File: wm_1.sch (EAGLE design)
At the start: 26 parts, among them IC2 DS1813-SMD, IC4 MEGA8-AI, T1 MMBT3904, T2 BT138-V, X1 MKDSN1,5/2-5,08, X2 MKDSN1,5/2-5,08

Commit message: wip
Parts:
- added R8, R9: 1k, rcl:R-EU_R1206
- added SJ1: (no value), MyLib:SOLDERJUMPERREFLOW
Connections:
- new net N$17: OK2.A, R8.1
- new net N$18: OK1.COL, R9.2, SJ1.1
- net +5V: now also R9.1
- net 485_R/W: now also R8.2; no longer OK2.A
- net GND: now also OK1.EMI
- net GROUND: now also R1.1, X1-2.KL; no longer R2.1, X1-1.KL
- net HOT: now also R2.1, X1-1.KL; no longer R1.1, X1-2.KL
- net INT0: now also SJ1.2
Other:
- moved on the sheet: X1-1, X1-2
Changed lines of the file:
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@@
 <part name="GND2" library="supply1" deviceset="GND" device=""/>
 <part name="OK2" library="MyLib" deviceset="MOC30*M" device="SMD" package3d_urn="urn:adsk.eagle:package:21970/1"/>
+<part name="R8" library="rcl" library_urn="urn:adsk.eagle:library:334" deviceset="R-EU_" device="R1206" package3d_urn="urn:adsk.eagle:package:23540/2" value="1k"/>
+<part name="R9" library="rcl" library_urn="urn:adsk.eagle:library:334" deviceset="R-EU_" device="R1206" package3d_urn="urn:adsk.eagle:package:23540/2" value="1k"/>
+<part name="P+1" library="supply1" deviceset="+5V" device=""/>
+<part name="SJ1" library="MyLib" deviceset="SOLDERJUMPER" device="REFLOW"/>
 </parts>
 <sheets>
@@
 <attribute name="VALUE" x="128.524" y="195.961" size="1.778" layer="96"/>
 </instance>
-<instance part="X1" gate="-1" x="347.98" y="177.8" smashed="yes">
-<attribute name="NAME" x="351.028" y="176.911" size="1.778" layer="95"/>
-<attribute name="VALUE" x="345.44" y="174.117" size="1.778" layer="96"/>
-</instance>
-<instance part="X1" gate="-2" x="347.98" y="170.18" smashed="yes">
+<instance part="X1" gate="-1" x="347.98" y="170.18" smashed="yes">
 <attribute name="NAME" x="351.028" y="169.291" size="1.778" layer="95"/>
 <attribute name="VALUE" x="345.44" y="166.497" size="1.778" layer="96"/>
+</instance>
+<instance part="X1" gate="-2" x="347.98" y="185.42" smashed="yes">
+<attribute name="NAME" x="351.028" y="184.531" size="1.778" layer="95"/>
+<attribute name="VALUE" x="345.44" y="181.737" size="1.778" layer="96"/>
 </instance>
 <instance part="IC4" gate="G$1" x="195.58" y="119.38" smashed="yes">
@@
 <attribute name="NAME" x="281.9146" y="160.6296" size="1.778" layer="95"/>
 <attribute name="VALUE" x="281.9146" y="142.3162" size="1.778" layer="96"/>
+</instance>
+<instance part="R8" gate="G$1" x="274.32" y="157.48" smashed="yes" rot="R180">
+<attribute name="NAME" x="278.13" y="155.9814" size="1.778" layer="95" rot="R180"/>
+<attribute name="VALUE" x="278.13" y="160.782" size="1.778" layer="96" rot="R180"/>
+</instance>
+<instance part="R9" gate="G$1" x="238.76" y="218.44" smashed="yes" rot="R270">
+<attribute name="NAME" x="240.2586" y="222.25" size="1.778" layer="95" rot="R270"/>
+<attribute name="VALUE" x="235.458" y="222.25" size="1.778" layer="96" rot="R270"/>
+</instance>
+<instance part="P+1" gate="1" x="238.76" y="231.14" smashed="yes">
+<attribute name="VALUE" x="236.22" y="226.06" size="1.778" layer="96" rot="R90"/>
+</instance>
+<instance part="SJ1" gate="1" x="256.54" y="208.28" smashed="yes">
+<attribute name="NAME" x="254" y="210.82" size="1.778" layer="95"/>
+<attribute name="VALUE" x="254" y="204.47" size="1.778" layer="96"/>
 </instance>
 </instances>
@@
 <label x="335.28" y="170.18" size="1.778" layer="95"/>
 <pinref part="R5" gate="G$1" pin="2"/>
+<pinref part="R6" gate="G$1" pin="1"/>
+<junction x="327.66" y="170.18"/>
+<pinref part="X1" gate="-1" pin="KL"/>
 <wire x1="340.36" y1="170.18" x2="345.44" y2="170.18" width="0.1524" layer="91"/>
 <junction x="340.36" y="170.18"/>
-<pinref part="R6" gate="G$1" pin="1"/>
-<junction x="327.66" y="170.18"/>
-<pinref part="X1" gate="-2" pin="KL"/>
-</segment>
-<segment>
-<pinref part="R1" gate="G$1" pin="1"/>
-<wire x1="111.76" y1="210.82" x2="93.98" y2="210.82" width="0.1524" layer="91"/>
-<label x="99.06" y="210.82" size="1.778" layer="95"/>
+</segment>
+<segment>
+<pinref part="R2" gate="G$1" pin="1"/>
+<wire x1="111.76" y1="190.5" x2="91.44" y2="190.5" width="0.1524" layer="91"/>
+<label x="96.52" y="190.5" size="1.778" layer="95"/>
 </segment>
 </net>
@@
 </segment>
 <segment>
-<pinref part="R2" gate="G$1" pin="1"/>
-<wire x1="111.76" y1="190.5" x2="93.98" y2="190.5" width="0.1524" layer="91"/>
-<label x="96.52" y="190.5" size="1.778" layer="95"/>
-</segment>
-<segment>
-<pinref part="X1" gate="-1" pin="KL"/>
-<wire x1="345.44" y1="177.8" x2="332.74" y2="177.8" width="0.1524" layer="91"/>
+<pinref part="X1" gate="-2" pin="KL"/>
+<wire x1="345.44" y1="185.42" x2="327.66" y2="185.42" width="0.1524" layer="91"/>
+<label x="330.2" y="185.42" size="1.778" layer="95"/>
+</segment>
+<segment>
+<pinref part="R1" gate="G$1" pin="1"/>
+<wire x1="111.76" y1="210.82" x2="91.44" y2="210.82" width="0.1524" layer="91"/>
+<label x="96.52" y="210.82" size="1.778" layer="95"/>
 </segment>
 </net>
@@
 <pinref part="OK2" gate="-1" pin="C"/>
 </segment>
+<segment>
+<pinref part="OK1" gate="G$1" pin="EMI"/>
+<pinref part="GND1" gate="1" pin="GND"/>
+<wire x1="231.14" y1="203.2" x2="231.14" y2="190.5" width="0.1524" layer="91"/>
+</segment>
 </net>
 <net name="SCL" class="0">
@@
 <wire x1="231.14" y1="116.84" x2="220.98" y2="116.84" width="0.1524" layer="91"/>
 <label x="226.06" y="116.84" size="1.778" layer="95"/>
+</segment>
+<segment>
+<pinref part="SJ1" gate="1" pin="2"/>
+<wire x1="261.62" y1="208.28" x2="276.86" y2="208.28" width="0.1524" layer="91"/>
+<label x="264.16" y="208.28" size="1.778" layer="95"/>
 </segment>
 </net>
@@
 <wire x1="134.62" y1="111.76" x2="134.62" y2="119.38" width="0.1524" layer="91"/>
 </segment>
+<segment>
+<pinref part="P+1" gate="1" pin="+5V"/>
+<pinref part="R9" gate="G$1" pin="1"/>
+<wire x1="238.76" y1="228.6" x2="238.76" y2="223.52" width="0.1524" layer="91"/>
+</segment>
 </net>
 <net name="SCK" class="0">
@@
 <pinref part="IC4" gate="G$1" pin="PD4(XCK/T0)"/>
 <wire x1="220.98" y1="111.76" x2="264.16" y2="111.76" width="0.1524" layer="91"/>
-<wire x1="279.4" y1="157.48" x2="264.16" y2="157.48" width="0.1524" layer="91"/>
 <wire x1="264.16" y1="157.48" x2="264.16" y2="111.76" width="0.1524" layer="91"/>
-<pinref part="OK2" gate="-1" pin="A"/>
+<pinref part="R8" gate="G$1" pin="2"/>
+<wire x1="269.24" y1="157.48" x2="264.16" y2="157.48" width="0.1524" layer="91"/>
 </segment>
 </net>
@@
 </segment>
 </net>
+<net name="N$17" class="0">
+<segment>
+<pinref part="OK2" gate="-1" pin="A"/>
+<pinref part="R8" gate="G$1" pin="1"/>
+</segment>
+</net>
+<net name="N$18" class="0">
+<segment>
+<pinref part="R9" gate="G$1" pin="2"/>
+<pinref part="OK1" gate="G$1" pin="COL"/>
+<wire x1="238.76" y1="213.36" x2="238.76" y2="208.28" width="0.1524" layer="91"/>
+<wire x1="238.76" y1="208.28" x2="231.14" y2="208.28" width="0.1524" layer="91"/>
+<wire x1="238.76" y1="208.28" x2="251.46" y2="208.28" width="0.1524" layer="91"/>
+<junction x="238.76" y="208.28"/>
+<pinref part="SJ1" gate="1" pin="1"/>
+</segment>
+</net>

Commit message: wip
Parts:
- removed X2: MKDSN1,5/2-5,08, con-phoenix-508:MKDSN1,5/2-5,08
- added HLK1: HLK-PM013W, hi-link:HLK-PM013W
- added OUT: MKDSN1,5/2-5,08, con-phoenix-508:MKDSN1,5/2-5,08
- added U$1: 2X16LCDSIDE, MyDisplays:2X16LCDSIDE
- renumbered X1 to IN
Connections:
- net 485_R/W renamed ON/OFF
- removed net N$10: IC4.PC0(ADC0)
- removed net N$11: IC4.PC1(ADC1)
- removed net N$12: IC4.PC2(ADC2)
- removed net N$13: IC4.PC3(ADC3)
- removed net SPI0: IC4.ADC6
- new net D4: IC4.PC0(ADC0), U$1.D4
- new net D5: IC4.PC1(ADC1), U$1.D5
- new net D6: IC4.PC2(ADC2), U$1.D6
- new net D7: IC4.PC3(ADC3), U$1.D7
- new net E: IC4.ADC7, U$1.E
- new net RS: IC4.ADC6, U$1.RS
- net +5V: now also HLK1.+VO
- net GND: now also HLK1.-VO
- net GROUND: now also HLK1.AC2, OUT-1.KL, R2.1; no longer R1.1, X2-2.KL
- net HOT: now also HLK1.AC1, R1.1; no longer R2.1
- net INT0: no longer SJ1.2
- net INT1: now also SJ1.2
- net LOAD: now also OUT-2.KL; no longer X2-1.KL

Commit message: wip
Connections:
- net N$14: no longer IC4.PB7(XTAL2/TOSC2)
- net N$26: no longer IC4.PB6(XTAL1/TOSC1)
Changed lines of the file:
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@@
 <pinref part="Q1" gate="G$1" pin="1"/>
 <pinref part="C18" gate="G$1" pin="1"/>
-<pinref part="IC4" gate="G$1" pin="PB7(XTAL2/TOSC2)"/>
-<wire x1="172.72" y1="121.92" x2="160.02" y2="121.92" width="0.1524" layer="91"/>
-<junction x="160.02" y="121.92"/>
 </segment>
 </net>
@@
 <pinref part="Q1" gate="G$1" pin="2"/>
 <pinref part="C17" gate="G$1" pin="2"/>
-<pinref part="IC4" gate="G$1" pin="PB6(XTAL1/TOSC1)"/>
-<wire x1="160.02" y1="127" x2="172.72" y2="127" width="0.1524" layer="91"/>
-<junction x="160.02" y="127"/>
 </segment>
 </net>

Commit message: wip
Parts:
- removed C16: 0.1, rcl:C-EUC0805
- removed C17, C18: (no value), rcl:C-EUC0805
- removed IC4: MEGA8-AI, atmel:MEGA8-AI
- removed Q1: (no value), crystal:CRYSTALSM49
- removed SJ1: (no value), MyLib:SOLDERJUMPERREFLOW
- removed U$1: 2X16LCDSIDE, MyDisplays:2X16LCDSIDE
- added IC1: TINY13-20MM0, atmel:TINY13-20MM0
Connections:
- removed net D4: IC4.PC0(ADC0), U$1.D4
- removed net D5: IC4.PC1(ADC1), U$1.D5
- removed net D6: IC4.PC2(ADC2), U$1.D6
- removed net D7: IC4.PC3(ADC3), U$1.D7
- removed net E: IC4.ADC7, U$1.E
- removed net E_RESET: IC4.PB1(OC1A)
- removed net E_SELECT: IC4.PB2(SS/OC1B)
- removed net INT0: IC4.PD2(INT0)
- removed net INT1: IC4.PD3(INT1), SJ1.2
- removed net N$14: C18.1, Q1.1
- removed net N$18: OK1.COL, R9.2, SJ1.1
- removed net N$26: C17.2, Q1.2
- removed net N$61: C16.1, IC4.AREF
- removed net N$64: IC4.PD6(AIN0)
- removed net N$66: IC4.PD5(T1)
- removed net RS: IC4.ADC6, U$1.RS
- removed net RXD: IC4.PD0(RXD)
- removed net SCL: IC4.PC5(ADC5/SCL)
- removed net SDA: IC4.PC4(ADC4/SDA)
- removed net SD_DETECT: IC4.PD7(AIN1)
- removed net SD_SELECT: IC4.PB0(ICP)
- removed net TXD: IC4.PD1(TXD)
- new net ZERO: OK1.COL, R9.2
- net +5V: now also IC1G$1.VCC; no longer IC4.AVCC, IC4.VCC@1, IC4.VCC@2
- net GND: now also IC1G$1.GND; no longer C16.2, C17.1, C18.2, IC4.GND, IC4.GND@1, IC4.GND@2
- net MISO: now also IC1G$1.PB1/PCINT1/AIN1/OC0B/INT0/MISO; no longer IC4.PB4(MISO)
- net MOSI: now also IC1G$1.PB0/PCINT0/AIN0/OC0A/MOSI; no longer IC4.PB3(MOSI/OC2)
- net ON/OFF: now also IC1G$1.PB4/PCINT4/ADC2; no longer IC4.PD4(XCK/T0)
- net RESET: now also IC1G$1.PB5/PCINT5/!RESET!/ADC0/DW; no longer IC4.PC6(/RESET)
- net SCK: now also IC1G$1.PB2/PCINT2/SCK/ADC1/T0; no longer IC4.PB5(SCK)
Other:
- moved on the sheet: IC2, JP1

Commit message: wip
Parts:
- removed HLK1: HLK-PM013W, hi-link:HLK-PM013W
- removed IC1: TINY13-20MM0, atmel:TINY13-20MM0
- removed IC2: DS1813-SMD, MyLib:DS1813-SMD
- removed R9: 1k, rcl:R-EU_R1206
- added F1: (no value), fuse:GSH15
- JP1: device pinhead:PINHD-2X3 -> pinhead:PINHD-1X3
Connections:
- net N$9 renamed GATE
- removed net +5V: HLK1.+VO, IC1G$1.VCC, IC2.+5V, JP1.2, R9.1
- removed net MISO: IC1G$1.PB1/PCINT1/AIN1/OC0B/INT0/MISO, JP1.1
- removed net MOSI: IC1G$1.PB0/PCINT0/AIN0/OC0A/MOSI, JP1.4
- removed net RESET: IC1G$1.PB5/PCINT5/!RESET!/ADC0/DW, IC2./RST, JP1.5
- removed net SCK: IC1G$1.PB2/PCINT2/SCK/ADC1/T0, JP1.3
- new net N$9: F1.2, IN-1.KL
- net GND: now also JP1.1; no longer HLK1.-VO, IC1G$1.GND, IC2.GND, JP1.6
- net GROUND: now also R1.1; no longer HLK1.AC2, R2.1
- net HOT: now also F1.1, R2.1; no longer HLK1.AC1, IN-1.KL, R1.1
- net ON/OFF: now also JP1.2; no longer IC1G$1.PB4/PCINT4/ADC2
- net ZERO: now also JP1.3; no longer R9.2
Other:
- moved on the sheet: B1, C1, C2, C3, C4, D1, IN-1, IN-2, OK1, OK2, OUT-1, OUT-2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

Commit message: First pcb revision
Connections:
- net HOT: no longer R2.1
- net N$9: now also R2.1
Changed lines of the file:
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@@
 <?xml version="1.0" encoding="utf-8"?>
 <!DOCTYPE eagle SYSTEM "eagle.dtd">
-<eagle version="9.3.0">
+<eagle version="9.2.2">
 <drawing>
 <settings>
@@
 <junction x="266.7" y="83.82"/>
 </segment>
-<segment>
-<pinref part="R2" gate="G$1" pin="1"/>
-<wire x1="40.64" y1="50.8" x2="15.24" y2="50.8" width="0.1524" layer="91"/>
-<label x="22.86" y="50.8" size="1.778" layer="95"/>
-</segment>
 </net>
 <net name="GROUND" class="0">
@@
 <pinref part="F1" gate="1" pin="2"/>
 <pinref part="IN" gate="-1" pin="KL"/>
-<wire x1="281.94" y1="83.82" x2="299.72" y2="83.82" width="0.1524" layer="91"/>
-</segment>
-</net>
+<wire x1="281.94" y1="83.82" x2="294.64" y2="83.82" width="0.1524" layer="91"/>
+<wire x1="294.64" y1="83.82" x2="299.72" y2="83.82" width="0.1524" layer="91"/>
+<wire x1="294.64" y1="83.82" x2="294.64" y2="22.86" width="0.1524" layer="91"/>
+<wire x1="294.64" y1="22.86" x2="33.02" y2="22.86" width="0.1524" layer="91"/>
+<wire x1="33.02" y1="22.86" x2="33.02" y2="50.8" width="0.1524" layer="91"/>
+<pinref part="R2" gate="G$1" pin="1"/>
+<wire x1="33.02" y1="50.8" x2="40.64" y2="50.8" width="0.1524" layer="91"/>
+</segment>
+</net>

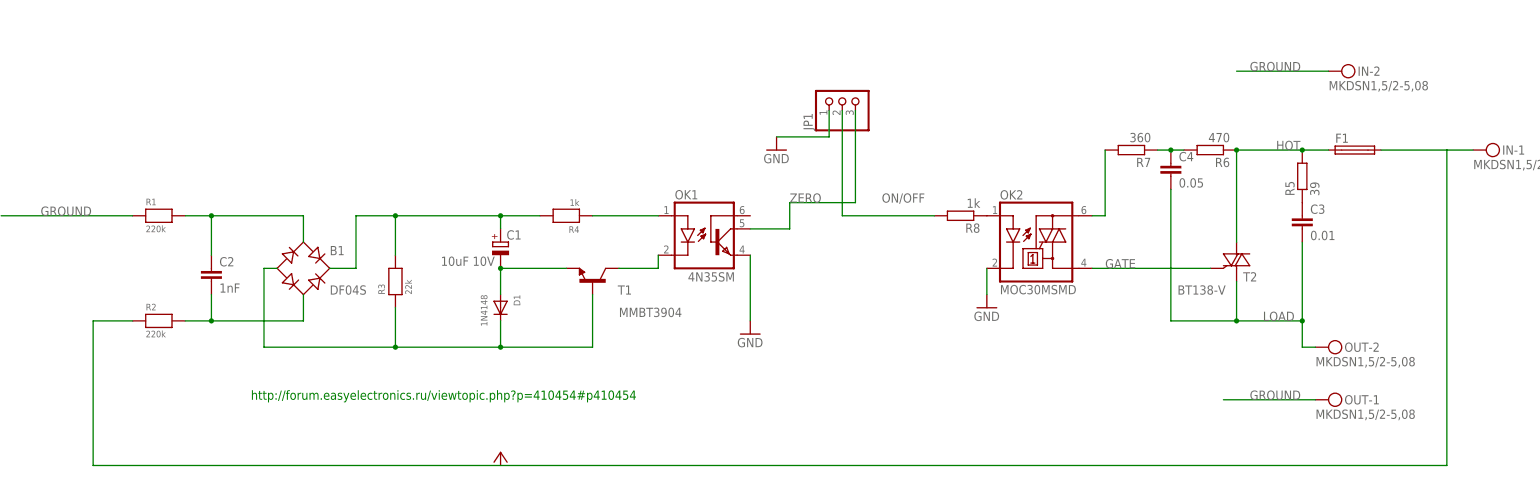
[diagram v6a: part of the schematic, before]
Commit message: Заменил разъем и сделал линии 0.5мм
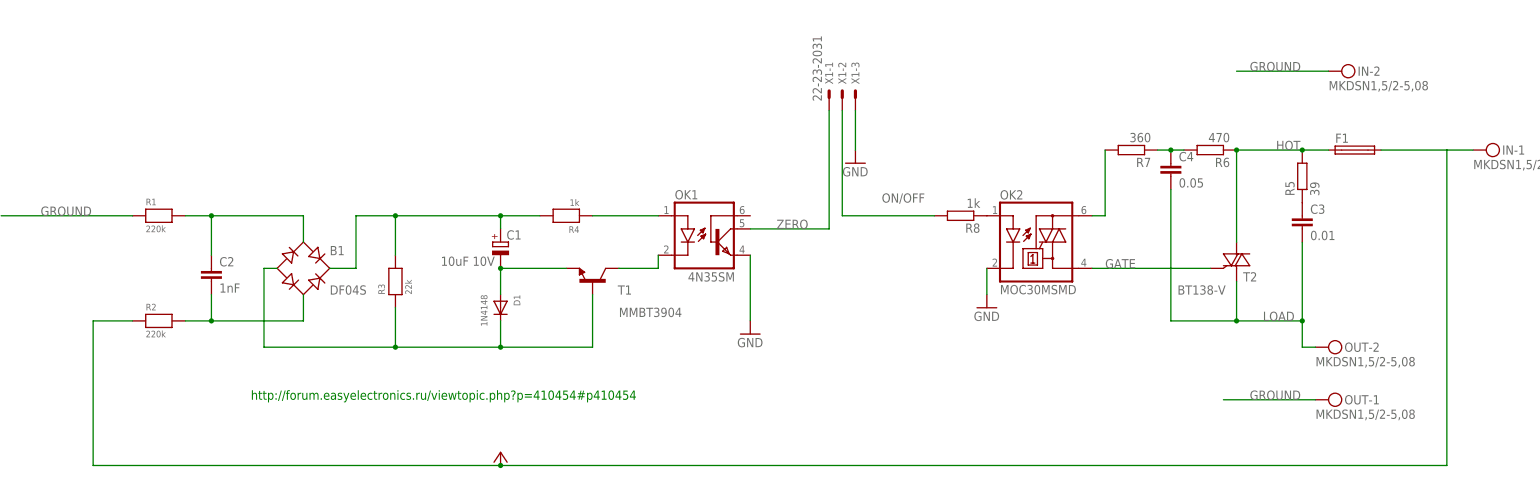
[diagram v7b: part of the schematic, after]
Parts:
- removed JP1: (no value), pinhead:PINHD-1X3
- added X1: 22-23-2031, con-molex:22-23-2031
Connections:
- net GND: now also X1-3.S; no longer JP1.1
- net ON/OFF: now also X1-2.S; no longer JP1.2
- net ZERO: now also X1-1.S; no longer JP1.3
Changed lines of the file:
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@@
 <?xml version="1.0" encoding="utf-8"?>
 <!DOCTYPE eagle SYSTEM "eagle.dtd">
-<eagle version="9.2.2">
+<eagle version="9.3.0">
 <drawing>
 <settings>
@@
 <part name="R8" library="rcl" library_urn="urn:adsk.eagle:library:334" deviceset="R-EU_" device="R1206" package3d_urn="urn:adsk.eagle:package:23540/2" value="1k"/>
 <part name="P+3" library="supply1" deviceset="+5V" device=""/>
-<part name="JP1" library="pinhead" library_urn="urn:adsk.eagle:library:325" deviceset="PINHD-1X3" device="" package3d_urn="urn:adsk.eagle:package:22458/2"/>
 <part name="GND3" library="supply1" deviceset="GND" device=""/>
 <part name="F1" library="fuse" library_urn="urn:adsk.eagle:library:233" deviceset="GSH15" device="" package3d_urn="urn:adsk.eagle:package:14065/1"/>
+<part name="X1" library="con-molex" library_urn="urn:adsk.eagle:library:165" deviceset="22-23-2031" device=""/>
 </parts>
 <sheets>
@@
 </instance>
 <instance part="P+3" gate="1" x="111.76" y="25.4" smashed="yes"/>
-<instance part="JP1" gate="A" x="177.8" y="93.98" smashed="yes" rot="R90">
-<attribute name="NAME" x="172.085" y="87.63" size="1.778" layer="95" rot="R90"/>
-<attribute name="VALUE" x="185.42" y="87.63" size="1.778" layer="96" rot="R90"/>
-</instance>
-<instance part="GND3" gate="1" x="165.1" y="83.82" smashed="yes">
-<attribute name="VALUE" x="162.56" y="81.28" size="1.778" layer="96"/>
+<instance part="GND3" gate="1" x="180.34" y="81.28" smashed="yes">
+<attribute name="VALUE" x="177.8" y="78.74" size="1.778" layer="96"/>
 </instance>
 <instance part="F1" gate="1" x="276.86" y="83.82" smashed="yes">
 <attribute name="NAME" x="273.05" y="85.217" size="1.778" layer="95"/>
 <attribute name="VALUE" x="273.05" y="80.899" size="1.778" layer="96"/>
+</instance>
+<instance part="X1" gate="-1" x="175.26" y="93.98" smashed="yes" rot="R90">
+<attribute name="NAME" x="176.022" y="96.52" size="1.524" layer="95" rot="R90"/>
+<attribute name="VALUE" x="173.863" y="93.218" size="1.778" layer="96" rot="R90"/>
+</instance>
+<instance part="X1" gate="-2" x="177.8" y="93.98" smashed="yes" rot="R90">
+<attribute name="NAME" x="178.562" y="96.52" size="1.524" layer="95" rot="R90"/>
+</instance>
+<instance part="X1" gate="-3" x="180.34" y="93.98" smashed="yes" rot="R90">
+<attribute name="NAME" x="181.102" y="96.52" size="1.524" layer="95" rot="R90"/>
 </instance>
 </instances>
@@
 </segment>
 <segment>
-<pinref part="JP1" gate="A" pin="1"/>
 <pinref part="GND3" gate="1" pin="GND"/>
-<wire x1="175.26" y1="91.44" x2="175.26" y2="86.36" width="0.1524" layer="91"/>
-<wire x1="175.26" y1="86.36" x2="165.1" y2="86.36" width="0.1524" layer="91"/>
+<wire x1="180.34" y1="91.44" x2="180.34" y2="83.82" width="0.1524" layer="91"/>
+<pinref part="X1" gate="-3" pin="S"/>
 </segment>
 </net>
@@
 <wire x1="195.58" y1="71.12" x2="177.8" y2="71.12" width="0.1524" layer="91"/>
 <label x="185.42" y="73.66" size="1.778" layer="95"/>
-<pinref part="JP1" gate="A" pin="2"/>
 <wire x1="177.8" y1="91.44" x2="177.8" y2="71.12" width="0.1524" layer="91"/>
+<pinref part="X1" gate="-2" pin="S"/>
 </segment>
 </net>
@@
 </segment>
 </net>
-<net name="ZERO" class="0">
-<segment>
-<pinref part="OK1" gate="G$1" pin="COL"/>
-<wire x1="167.64" y1="73.66" x2="167.64" y2="68.58" width="0.1524" layer="91"/>
-<wire x1="167.64" y1="68.58" x2="160.02" y2="68.58" width="0.1524" layer="91"/>
-<label x="167.64" y="73.66" size="1.778" layer="95"/>
-<pinref part="JP1" gate="A" pin="3"/>
-<wire x1="180.34" y1="91.44" x2="180.34" y2="73.66" width="0.1524" layer="91"/>
-<wire x1="180.34" y1="73.66" x2="167.64" y2="73.66" width="0.1524" layer="91"/>
-</segment>
-</net>
 <net name="N$9" class="0">
 <segment>
@@
 <wire x1="294.64" y1="83.82" x2="299.72" y2="83.82" width="0.1524" layer="91"/>
 <wire x1="294.64" y1="83.82" x2="294.64" y2="22.86" width="0.1524" layer="91"/>
-<wire x1="294.64" y1="22.86" x2="33.02" y2="22.86" width="0.1524" layer="91"/>
+<wire x1="294.64" y1="22.86" x2="111.76" y2="22.86" width="0.1524" layer="91"/>
+<wire x1="111.76" y1="22.86" x2="33.02" y2="22.86" width="0.1524" layer="91"/>
 <wire x1="33.02" y1="22.86" x2="33.02" y2="50.8" width="0.1524" layer="91"/>
 <pinref part="R2" gate="G$1" pin="1"/>
 <wire x1="33.02" y1="50.8" x2="40.64" y2="50.8" width="0.1524" layer="91"/>
-</segment>
-</net>
+<pinref part="P+3" gate="1" pin="+5V"/>
+<junction x="111.76" y="22.86"/>
+</segment>
+</net>
+<net name="ZERO" class="0">
+<segment>
+<pinref part="OK1" gate="G$1" pin="COL"/>
+<wire x1="160.02" y1="68.58" x2="175.26" y2="68.58" width="0.1524" layer="91"/>
+<wire x1="175.26" y1="68.58" x2="175.26" y2="91.44" width="0.1524" layer="91"/>
+<label x="165.1" y="68.58" size="1.778" layer="95"/>
+<pinref part="X1" gate="-1" pin="S"/>
+</segment>
+</net>

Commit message: first revision
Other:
- note added: "220V"
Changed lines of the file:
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@@
 <plain>
 <text x="63.5" y="35.56" size="1.778" layer="91">http://forum.easyelectronics.ru/viewtopic.php?p=410454#p410454</text>
+<text x="38.1" y="60.96" size="1.778" layer="91">220V</text>
 </plain>
 <instances>
